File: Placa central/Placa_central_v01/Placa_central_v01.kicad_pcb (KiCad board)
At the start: 2 copper layers, 69 parts, among them J1 PinoCheckBateriaVcc, J10 Conn_01x01_Arduino11, J11 Conn_01x01_Arduino12, J12 Conn_01x01_Arduino13, J13 Conn_01x01_Arduino14, J14 Conn_01x01_Arduino15, J15 Conn_01x01_Arduino16, J16 Conn_01x01_Motor1PonteHPCB, J17 PinoChargeBateriaGND, J18 Conn_01x01_Arduino19, J19 Conn_01x01_Arduino20, J2 Conn_01x02_ArduinoTxRx, J20 Conn_01x01_Arduino21, J21 Conn_01x01_Arduino22, J22 Conn_01x01_Arduino23, J23 Conn_01x01_Arduino24, J24 Conn_01x01_Arduino25, J25 Conn_01x01_Arduino26, J26 Conn_02x08_Odd_Even, J27 Conn_01x01_Motor2PonteHPCB, J28 Conn_01x01_Motor1PCBMotor, J29 Conn_01x01_Motor2PCBMotor, J3 Conn_01x01_ArduinoReset, J37 Conn_01x01_8.4VPonteH, J38 Conn_01x01_5VPonteH, J39 Conn_01x01_GNDPonteH, J4 Conn_01x01_Arduino5, J40 Conn_01x01_Motor1PWM, J41 Conn_01x01_Motor1Dir1, J42 Conn_01x01_Motor1Dir2, J43 Conn_01x01_Motor2Dir1, J44 Conn_01x01_Motor2Dir2, J45 Conn_01x01_Motor2PWM, J48 Conn_01x01_5VEncoderEsq, J49 Conn_01x01_OutputEncoderEsq, J5 Conn_01x01_Arduino6, J50 Conn_01x01_GNDEncoderEsq, J51 Conn_01x01_5VEncoderDir, J52 Conn_01x01_OutputEncoderDir, J53 Conn_01x01_GNDEncoderDir, J6 Conn_01x01_Arduino7, J7 Conn_01x01_Arduino8, J8 Conn_01x01_Arduino9, J9 Conn_01x01_Arduino10, Q1 BC548, Q2 BC548, SW1 SW_ON/OFF, SW3 SW_comando1

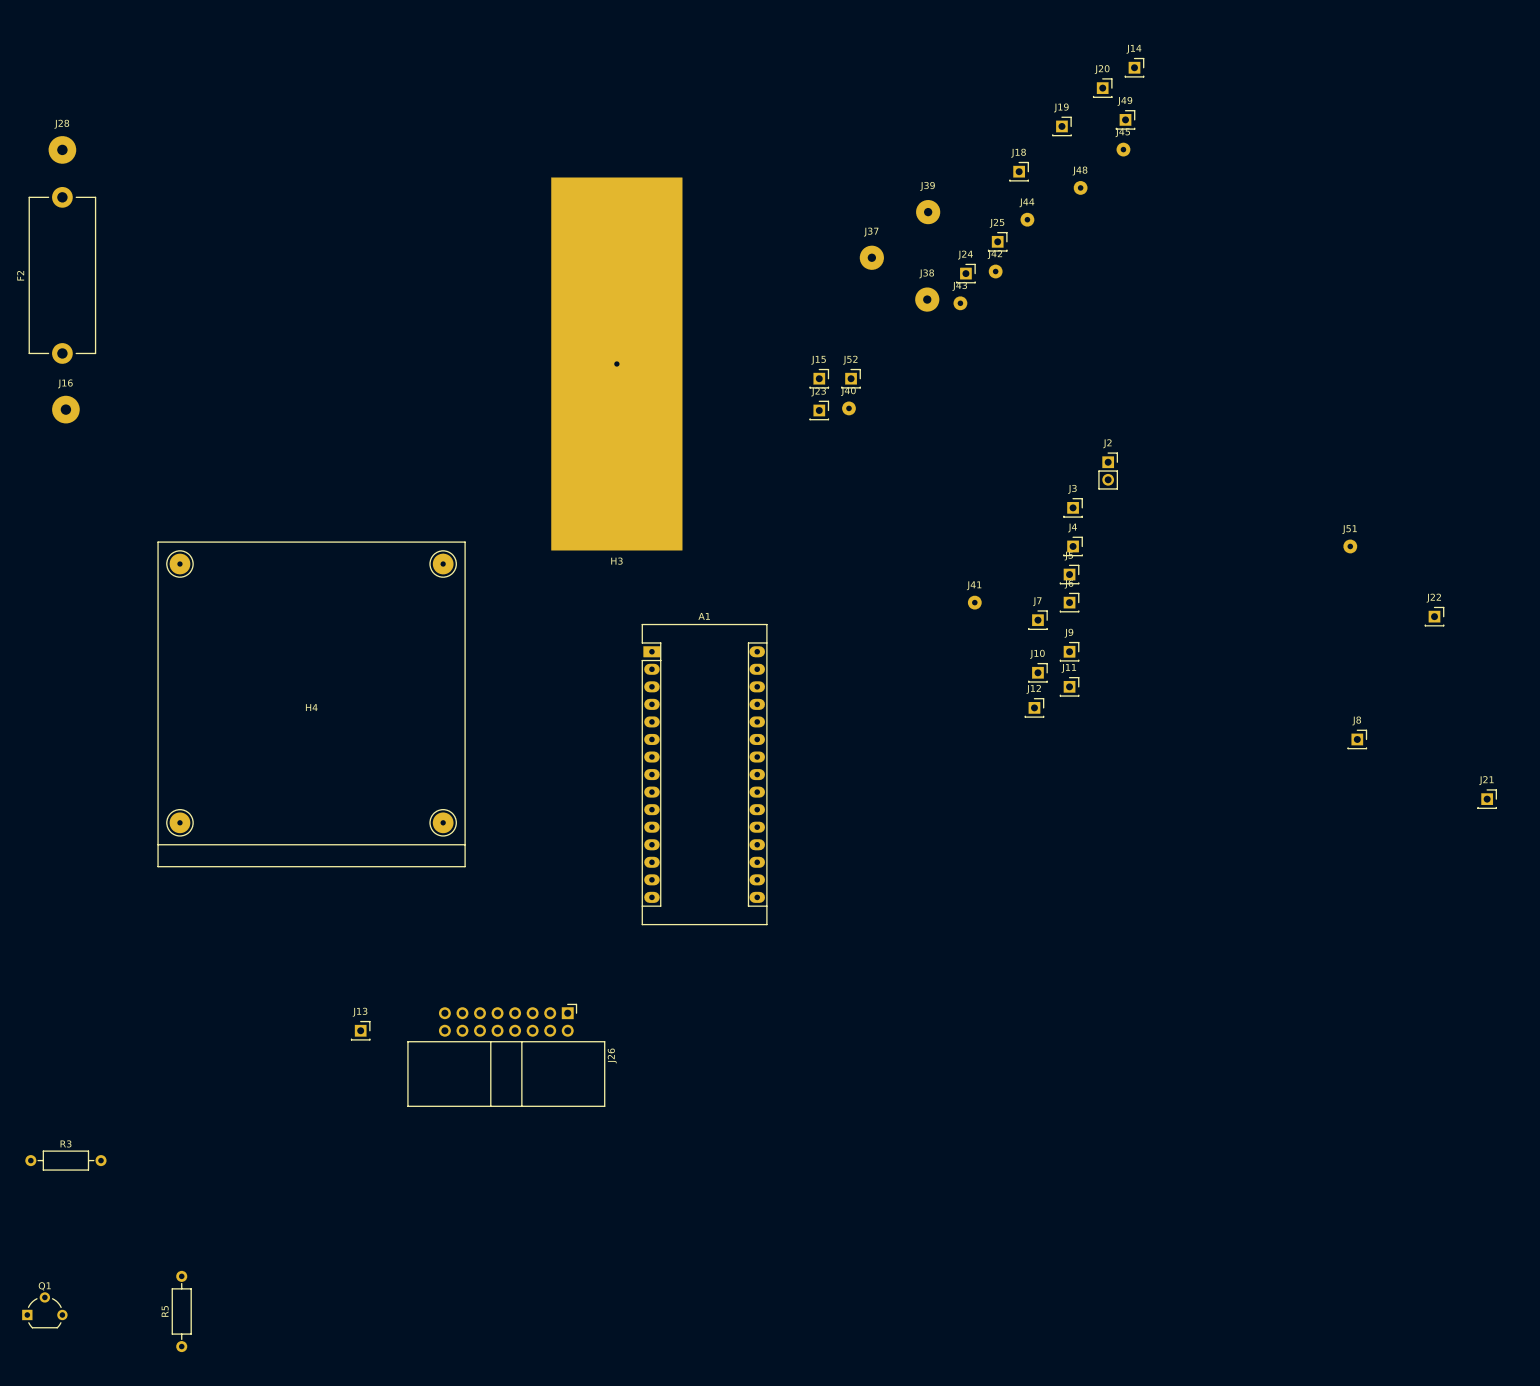
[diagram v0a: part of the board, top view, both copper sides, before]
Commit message: Bordas da PCB delimitadas e pinos agrupados
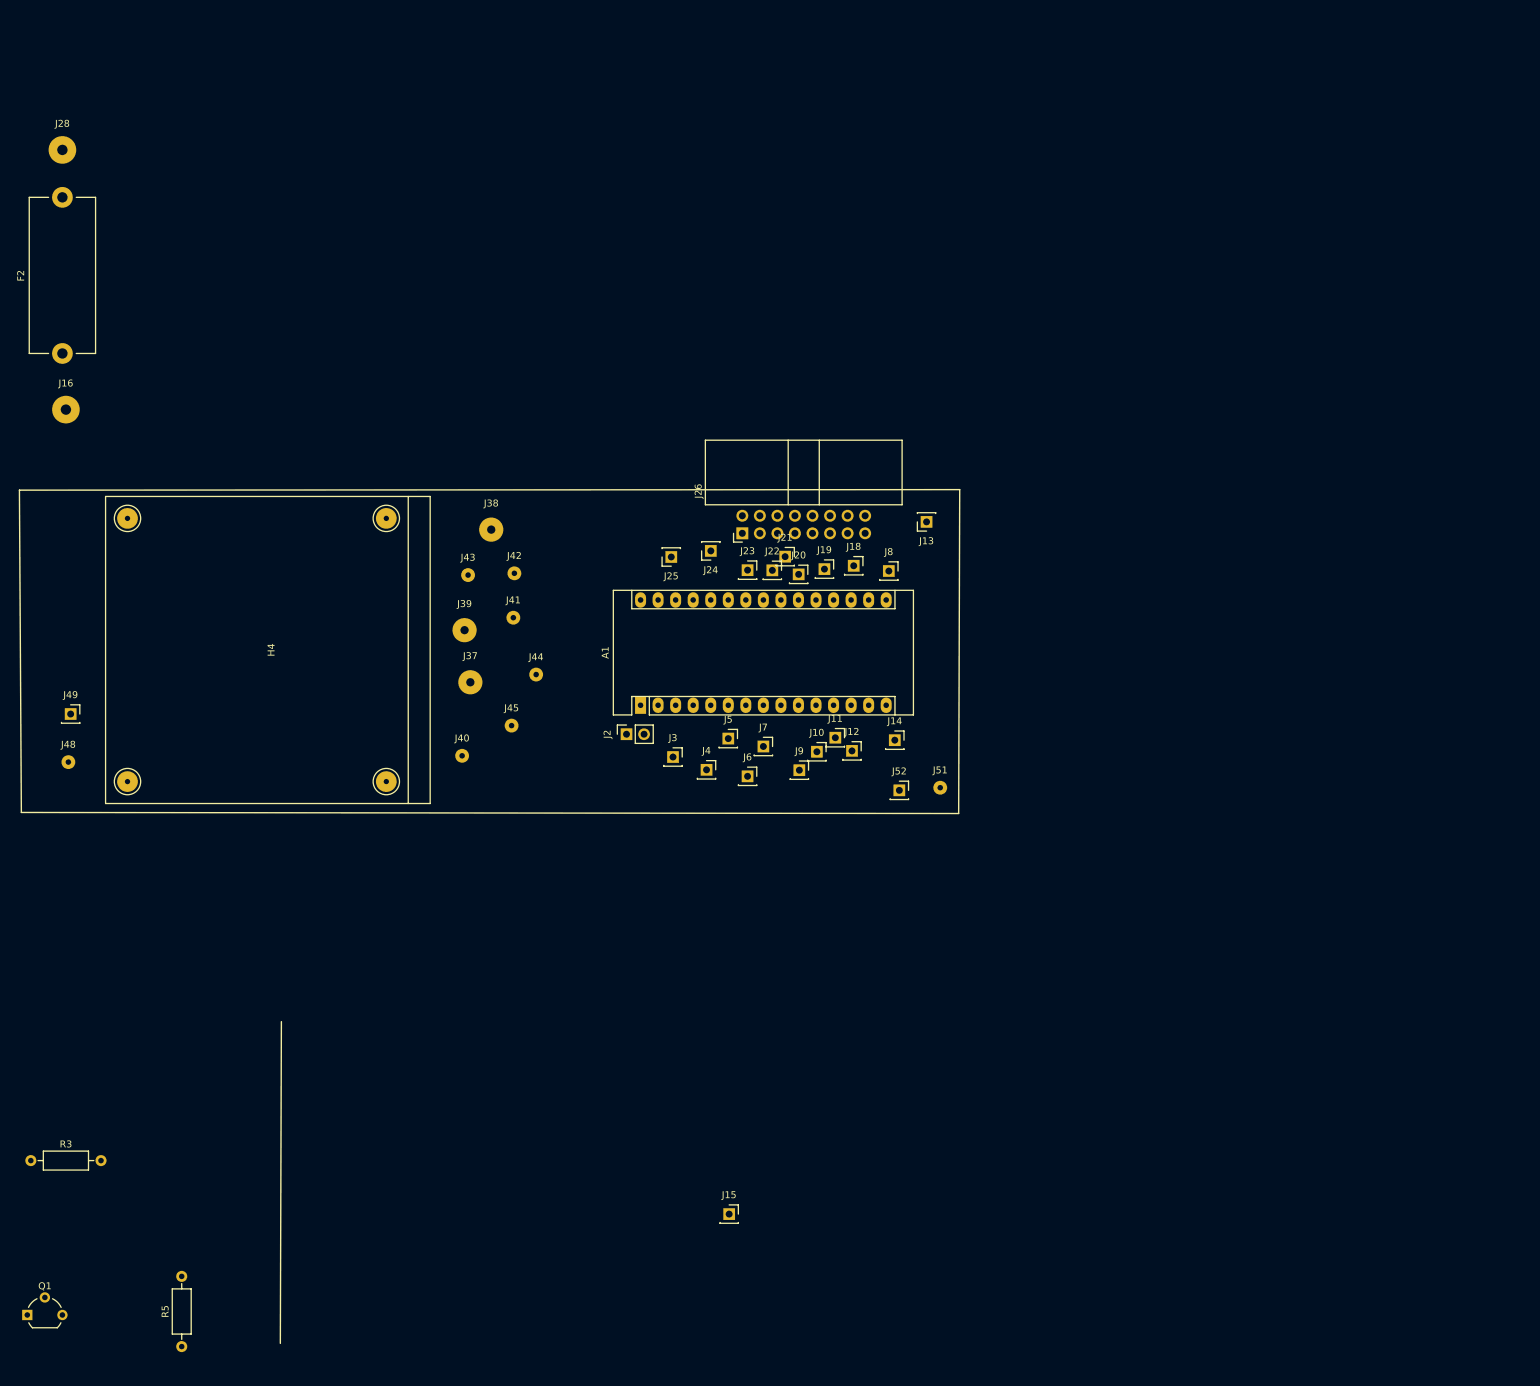
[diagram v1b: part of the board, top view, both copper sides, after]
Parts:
- removed H3: FuroBateria, Sensores_e_componentes_SL:Bateria
- J17: value PinoChargeBateriaGND -> PinoCheckBateriaGND
- moved J49 175.3 mm to (34.2, 93.9)
- moved J48 168.5 mm to (33.9, 100.8)
- moved J45 121.6 mm to (98.0, 95.5)
- moved J15 121.6 mm to (129.5, 166.2)
- moved J13 110.2 mm to (158.1, 66.0), turned to 180 degrees
- moved J21 107.5 mm to (137.6, 71.1)
- moved J14 103.3 mm to (153.5, 97.6)
- moved J44 96.9 mm to (101.6, 88.1)
- moved J22 96.1 mm to (135.8, 73.1)
- moved J39 90.4 mm to (91.2, 81.7)
- moved J37 84.6 mm to (92.1, 89.3)
- moved J20 83.0 mm to (139.6, 73.6)
- moved J42 82.2 mm to (98.5, 73.5)
- moved J43 81.4 mm to (91.7, 73.7)
- moved J2 80.1 mm to (114.7, 96.8), turned to 90 degrees
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
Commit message: Componentes quase todos posicionados, ainda não pronto para root
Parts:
- J37: footprint Connector_Wire:SolderWirePad_1x01_Drill1.2mm -> Wire_Pads:SolderWirePad_single_1-2mmDrill
- SW1: footprint Sensores_e_componentes_SL:BotaoOnOff -> CUSTOM_Placa_central_v01:Solder_Pad_Custom
- moved H2 632.2 mm to (18.7, 176.8)
- moved J17 625.6 mm to (24.9, 176.8)
- moved SW1 500.0 mm to (103.8, 110.1)
- moved D1 389.8 mm to (212.2, 115.3)
- moved F1 377.0 mm to (246.9, 133.8)
- moved H1 373.7 mm to (252.6, 113.4)
- moved R1 369.0 mm to (232.2, 142.9)
- moved J1 369.0 mm to (242.3, 153.5)
- moved D4 330.1 mm to (102.6, 68.3), turned to 90 degrees
- moved D5 311.9 mm to (109.2, 64.8), turned to 180 degrees
- moved R7 300.8 mm to (113.1, 65.1)
- moved R6 281.8 mm to (110.2, 70.9)
- moved RPullDown1 229.3 mm to (98.8, 94.2)
- moved SW3 197.1 mm to (101.1, 85.1)
- moved J29 189.4 mm to (274.6, 32.2)
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
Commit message: feita a divisão de placas, pinos extras pendentes
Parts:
- moved J16 233.5 mm to (266.9, 56.1), turned to 90 degrees
- moved F2 226.3 mm to (258.8, 56.6), turned to 180 degrees
- moved J28 201.3 mm to (229.3, 56.6), turned to 90 degrees
- moved J1 118.1 mm to (138.3, 97.8)
- moved R4 117.3 mm to (104.4, 85.4), turned to 180 degrees
- moved H1 117.0 mm to (136.0, 104.1)
- moved D2 112.4 mm to (106.9, 98.1)
- moved R1 111.0 mm to (138.4, 83.4)
- moved Q2 105.0 mm to (97.4, 94.3), turned to 90 degrees
- moved R2 105.0 mm to (79.6, 95.0)
- moved F1 104.7 mm to (146.2, 105.0), turned to 90 degrees
- moved J17 103.6 mm to (76.7, 87.0)
- moved H2 101.7 mm to (69.9, 88.8)
- moved D3 99.6 mm to (102.9, 93.8), turned to 0 degrees
- moved Q1 94.2 mm to (88.4, 87.5), turned to 180 degrees
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
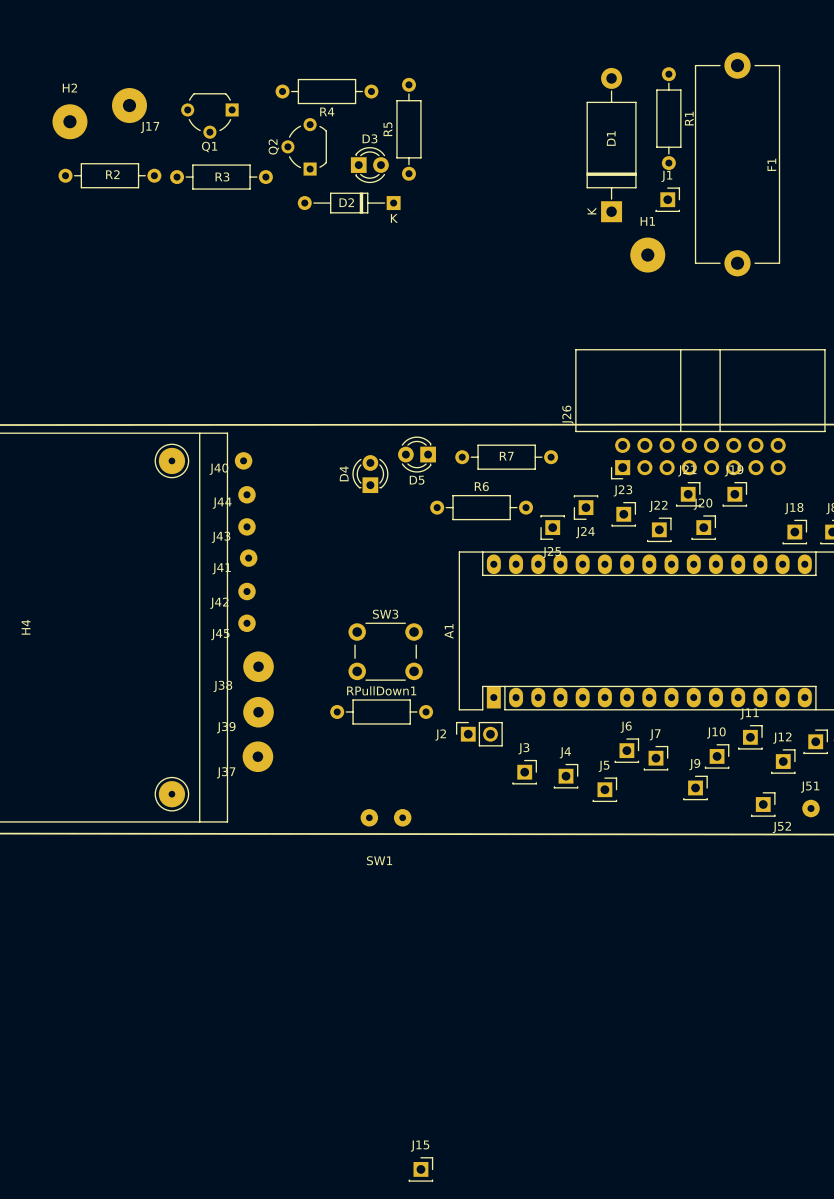
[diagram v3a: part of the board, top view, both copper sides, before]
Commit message: Circuito medidor de bateria aglutinado a placa central
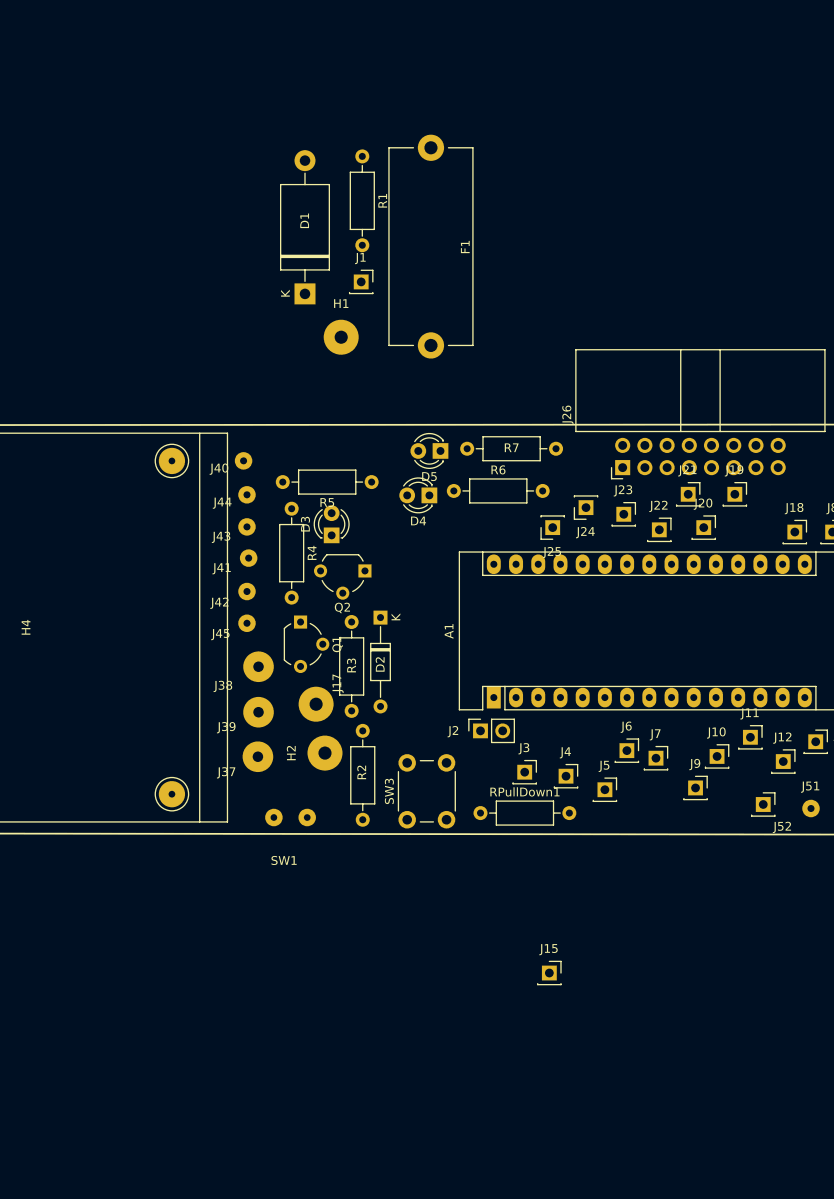
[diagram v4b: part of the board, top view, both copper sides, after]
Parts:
- moved H2 77.9 mm to (99.1, 161.0), turned to 90 degrees
- moved J17 71.7 mm to (98.0, 155.4), turned to 90 degrees
- moved R2 67.8 mm to (103.4, 158.5), turned to 270 degrees
- moved Q1 59.1 mm to (96.3, 146.1), turned to 270 degrees
- moved R3 51.8 mm to (102.1, 146.1), turned to 270 degrees
- moved R4 48.6 mm to (95.2, 133.1), turned to 270 degrees
- moved D2 47.4 mm to (105.4, 145.5), turned to 270 degrees
- moved Q2 46.4 mm to (103.6, 140.2), turned to 180 degrees
- moved D3 42.5 mm to (99.8, 136.1), turned to 90 degrees
- moved F1 36.3 mm to (111.2, 114.4)
- moved D1 36.3 mm to (96.8, 108.5)
- moved H1 36.3 mm to (100.9, 113.5)
- moved J1 36.3 mm to (103.2, 107.2)
- moved R1 36.3 mm to (103.3, 92.8)
- moved R5 35.5 mm to (104.4, 130.0), turned to 180 degrees
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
